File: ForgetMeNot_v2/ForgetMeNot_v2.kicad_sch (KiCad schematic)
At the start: 29 parts, among them J1 ISP Connector, SW1 SW_Push, U1 ATmega328PB-M, U4 LIS2HH12, U5 MCP1640x-xMC

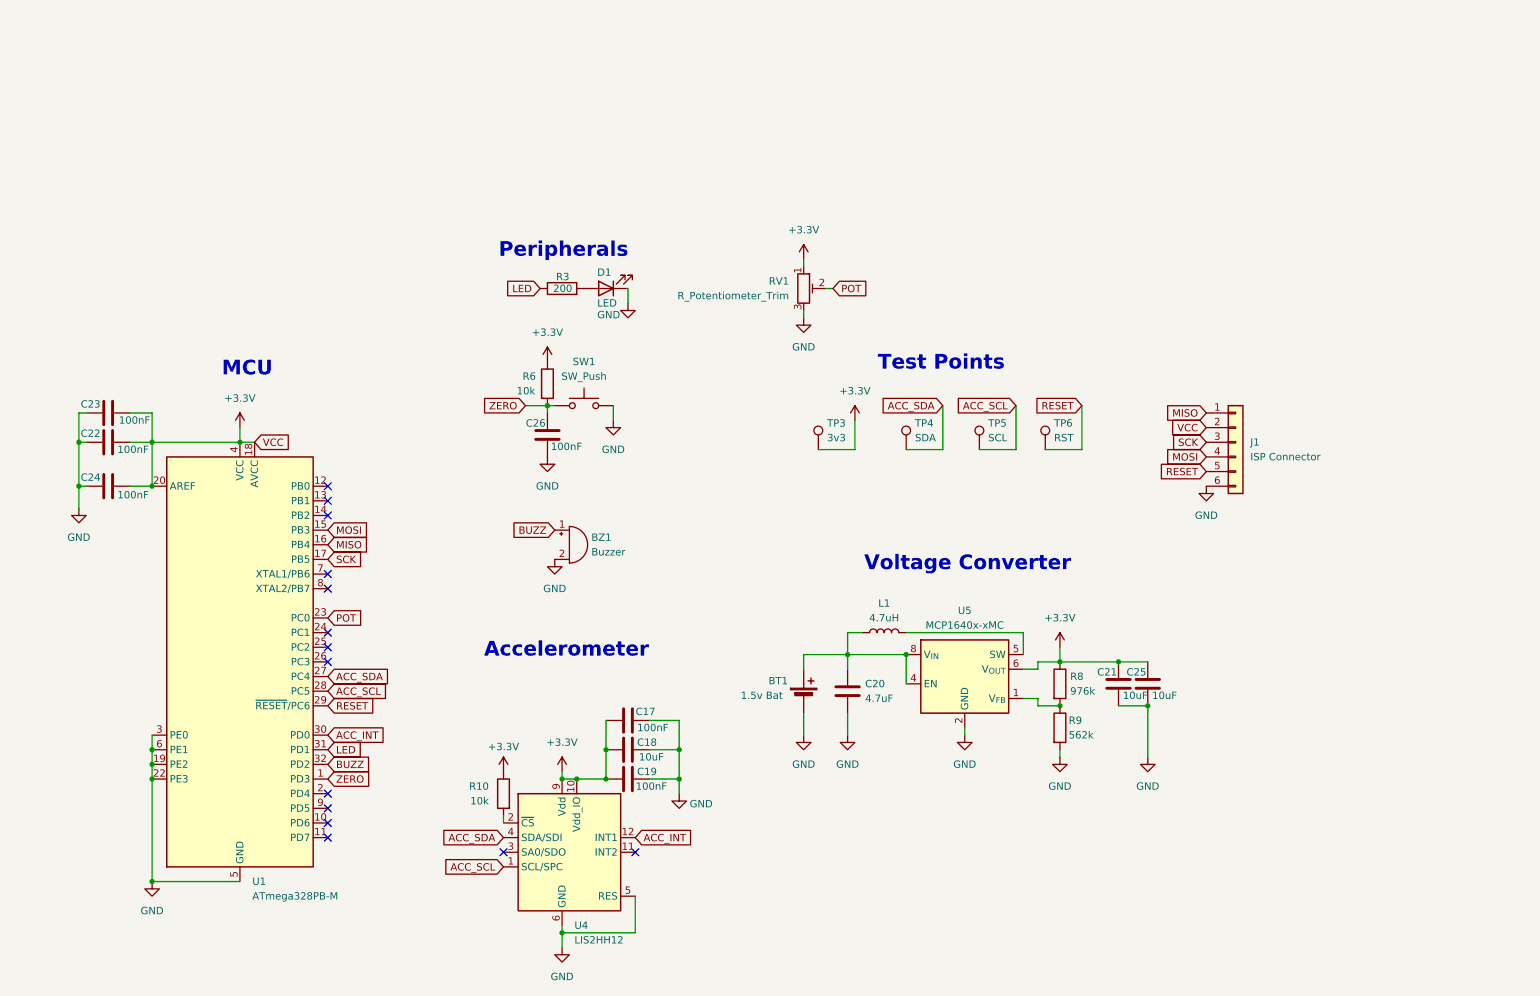
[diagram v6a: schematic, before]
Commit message: swapped connector for solder pads
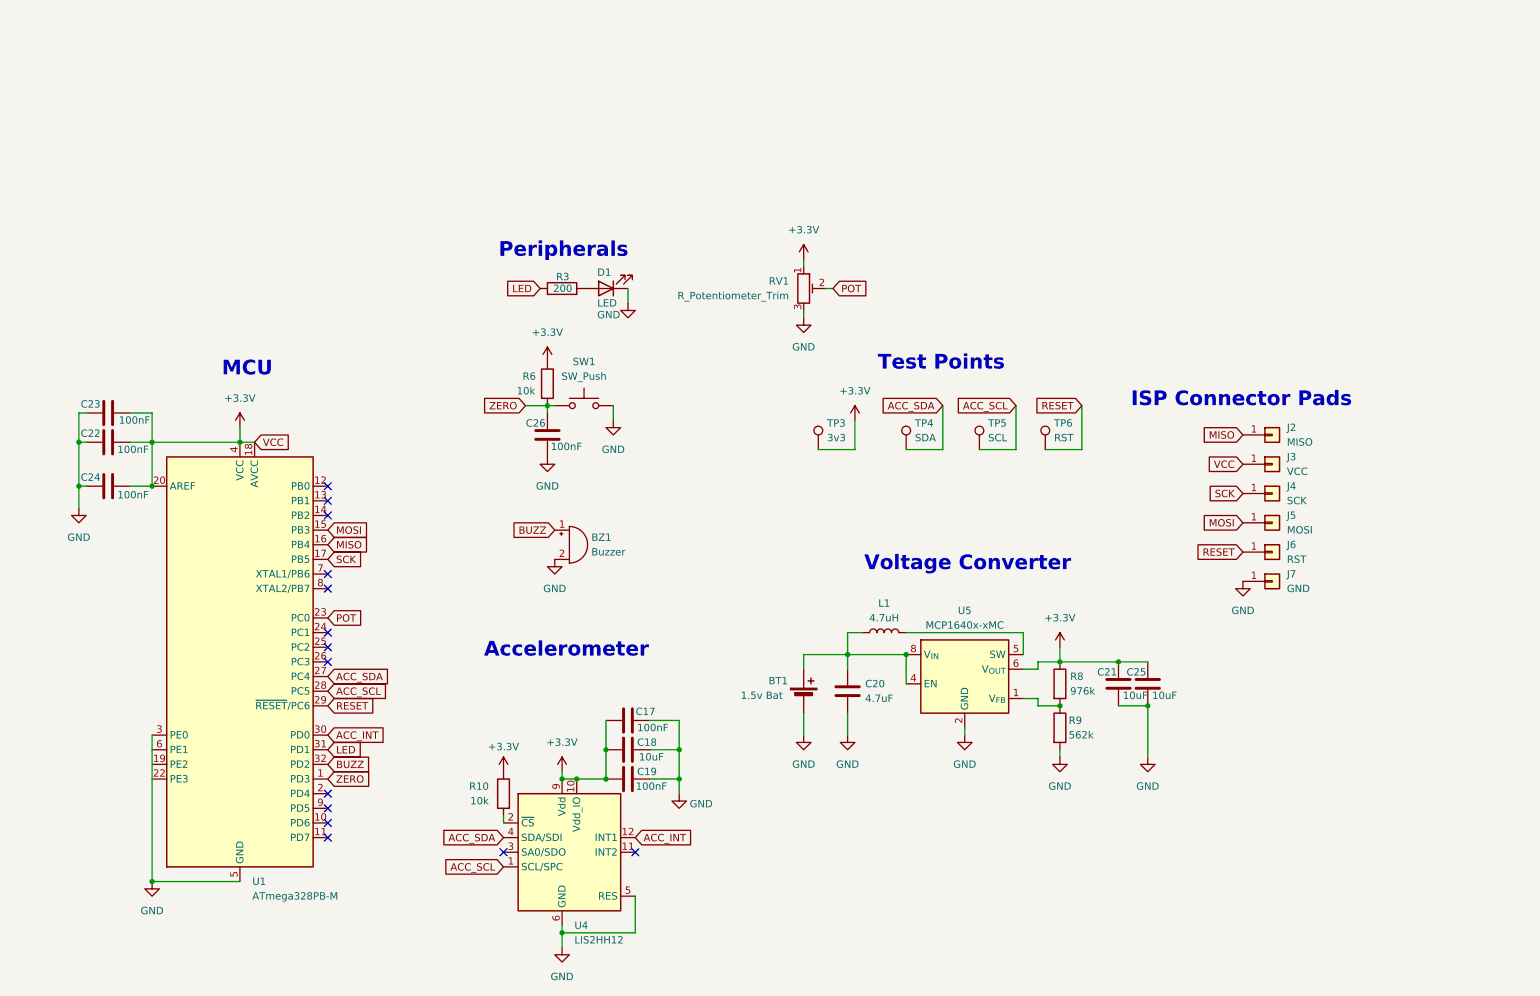
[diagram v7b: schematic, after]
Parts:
- removed J1: ISP Connector, Connector_Molex:Molex_Micro-Latch_53254-0670_1x06_P2.00mm_Horizontal, symbol Connector_Generic:Conn_01x06
- added J2: MISO, Connector_Wire:SolderWirePad_1x01_SMD_3x6mm, symbol Connector_Generic:Conn_01x01
- added J3: VCC, Connector_Wire:SolderWirePad_1x01_SMD_3x6mm, symbol Connector_Generic:Conn_01x01
- added J4: SCK, Connector_Wire:SolderWirePad_1x01_SMD_3x6mm, symbol Connector_Generic:Conn_01x01
- added J5: MOSI, Connector_Wire:SolderWirePad_1x01_SMD_3x6mm, symbol Connector_Generic:Conn_01x01
- added J6: RST, Connector_Wire:SolderWirePad_1x01_SMD_3x6mm, symbol Connector_Generic:Conn_01x01
- added J7: GND, Connector_Wire:SolderWirePad_1x01_SMD_3x6mm, symbol Connector_Generic:Conn_01x01
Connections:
- net +3.3V: now also J3.1 (Pin_1)
- net GND: now also J7.1 (Pin_1); no longer U1.19 (PE2), U1.22 (PE3), U1.6 (PE1)
- net MISO: now also J2.1 (Pin_1)
- net MOSI: now also J5.1 (Pin_1)
- net RESET: now also J6.1 (Pin_1)
- net SCK: now also J4.1 (Pin_1)
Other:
- note added: "ISP Connector Pads"
